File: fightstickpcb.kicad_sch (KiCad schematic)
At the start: 0 parts

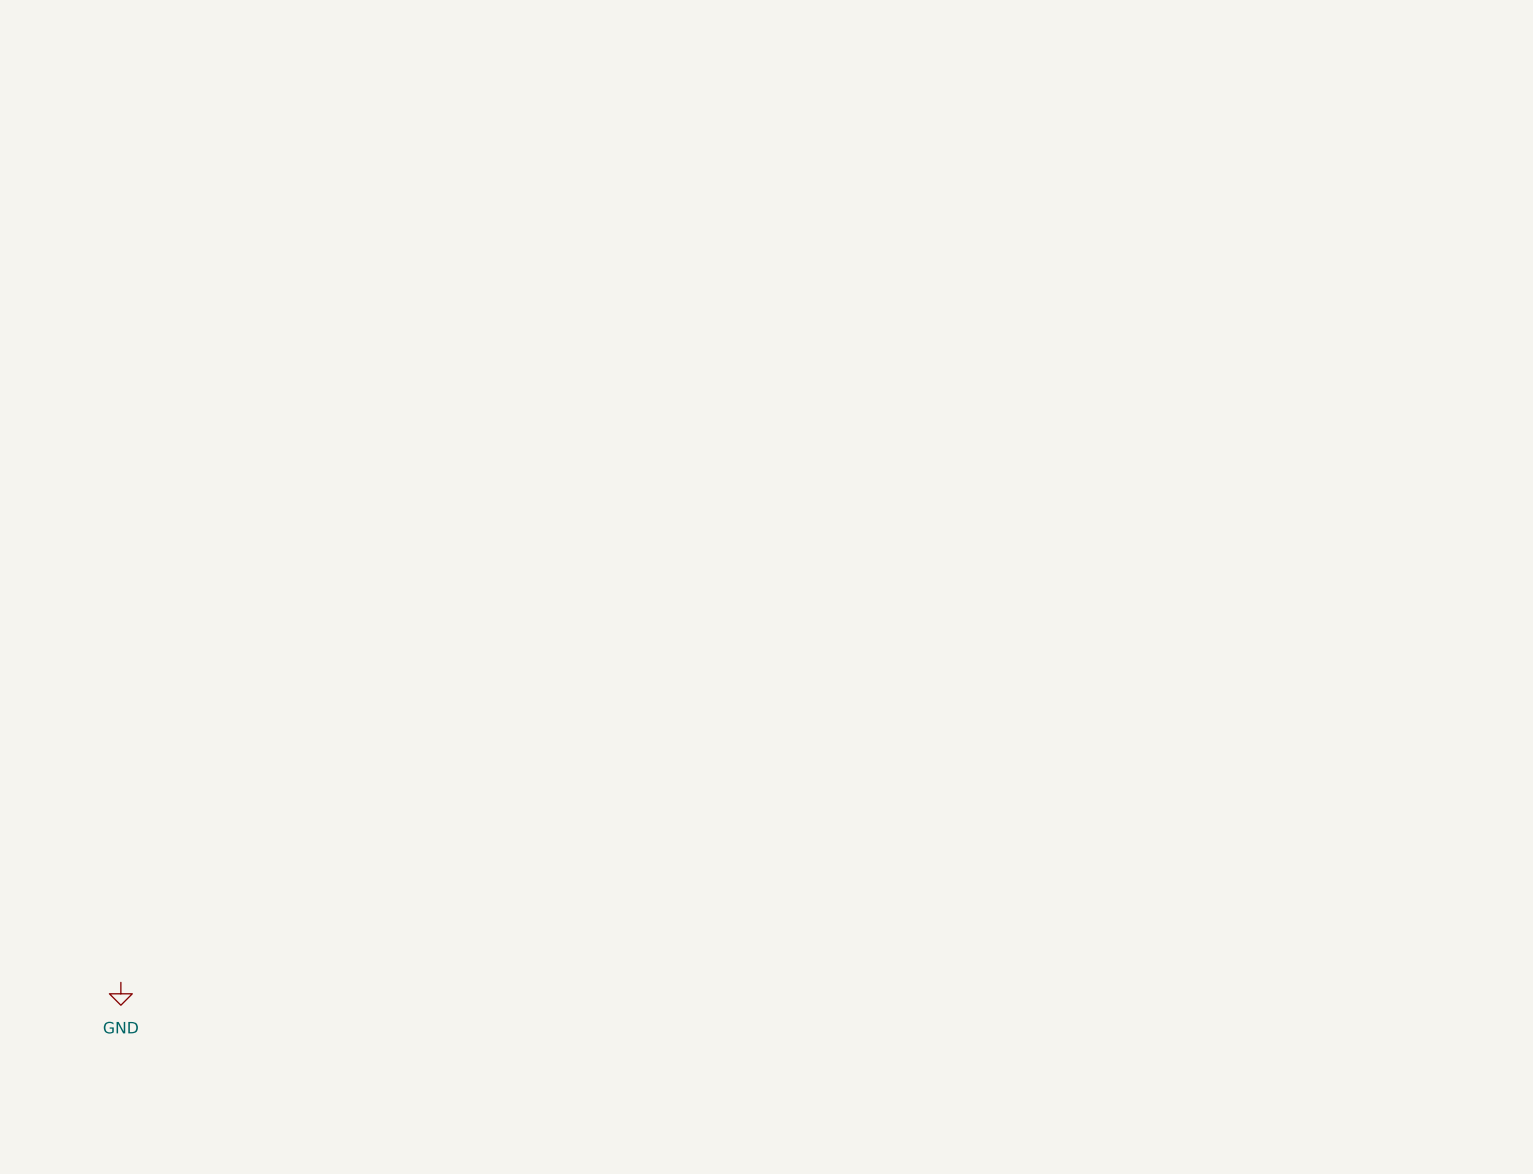
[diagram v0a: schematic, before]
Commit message: worked pcb and added switches power and pico. TODO: add pull up resistors to the schematic.
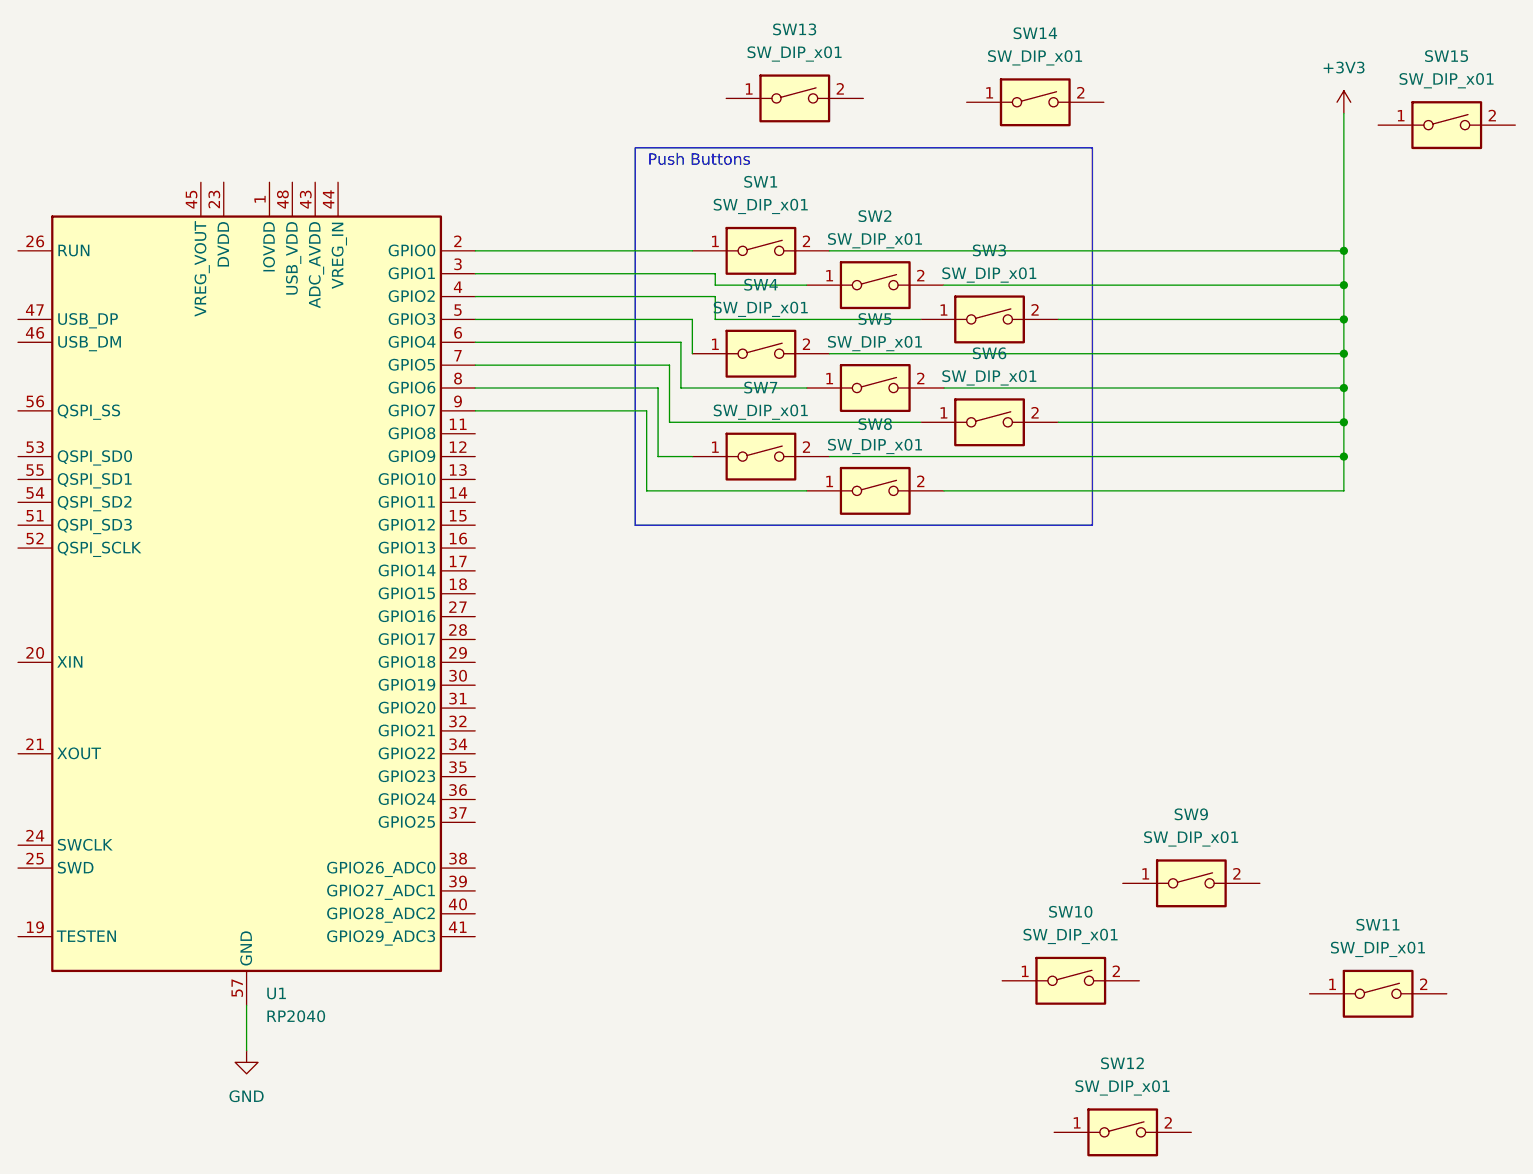
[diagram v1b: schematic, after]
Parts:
- added SW1, SW10, SW11, SW12, SW13, SW14, SW15, SW2, SW3, SW4, SW5, SW6, SW7, SW8, SW9: SW_DIP_x01, symbol Switch:SW_DIP_x01
- added U1: RP2040, Package_DFN_QFN:QFN-56-1EP_7x7mm_P0.4mm_EP3.2x3.2mm, symbol MCU_RaspberryPi:RP2040
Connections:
- net GND: now also U1.57 (GND)
- new net: SW5.1, U1.6 (GPIO4)
- new net: SW7.1, U1.8 (GPIO6)
- new net: SW1.1, U1.2 (GPIO0)
- new net: SW2.1, U1.3 (GPIO1)
- new net: SW6.1, U1.7 (GPIO5)
- new net: SW3.1, U1.4 (GPIO2)
- new net: SW4.1, U1.5 (GPIO3)
- new net: SW8.1, U1.9 (GPIO7)
- new net: U1.1 (IOVDD), U1.10 (IOVDD), U1.22 (IOVDD), U1.33 (IOVDD), U1.42 (IOVDD), U1.49 (IOVDD)
- new net: U1.23 (DVDD), U1.50 (DVDD)
- new net +3V3: SW1.2, SW2.2, SW3.2, SW4.2, SW5.2, SW6.2, SW7.2, SW8.2
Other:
- note added: "Push Buttons"
